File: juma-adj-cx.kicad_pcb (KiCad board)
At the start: 2 copper layers, 90 x 40 mm, 18 parts, among them J1 IN+, J2 IN-, J3 OUT+, J4 OUT-, Q1 BD139, Q2 2SC5200

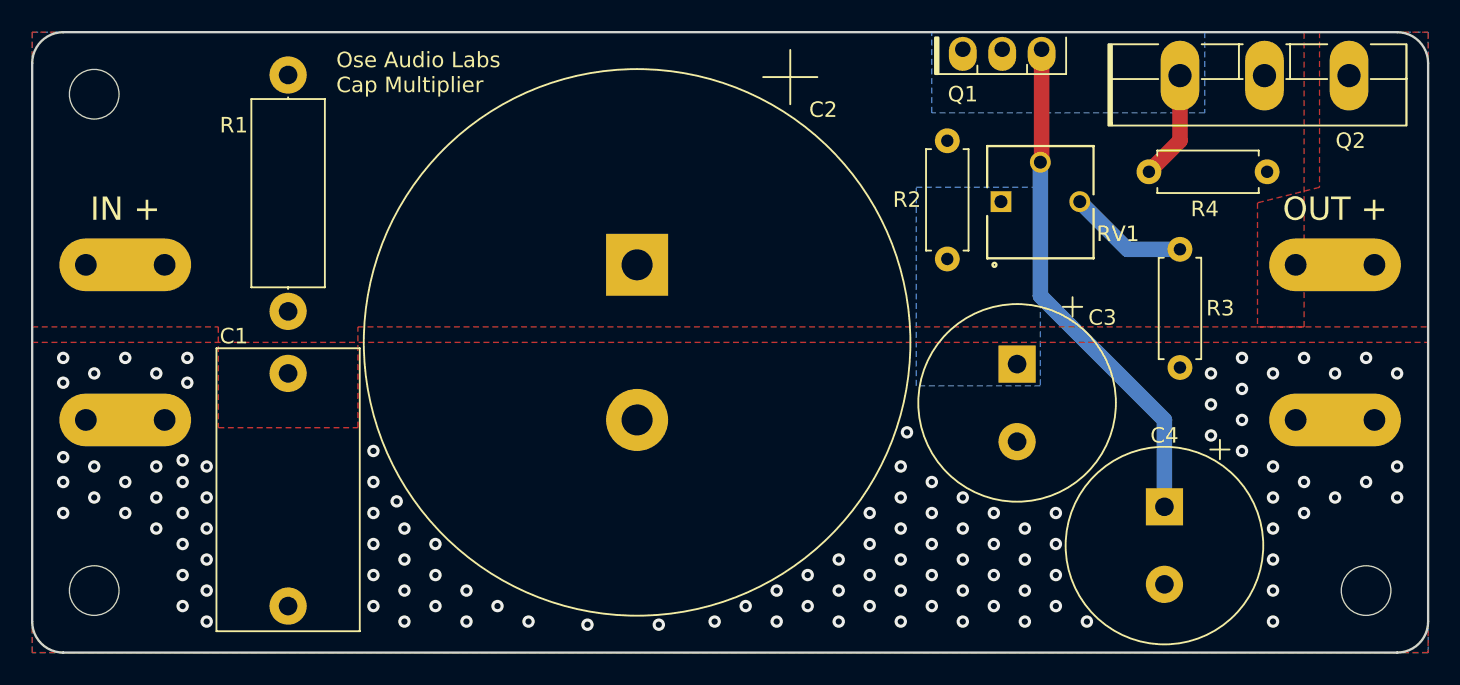
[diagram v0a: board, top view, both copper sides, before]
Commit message: separate in/out ground planes
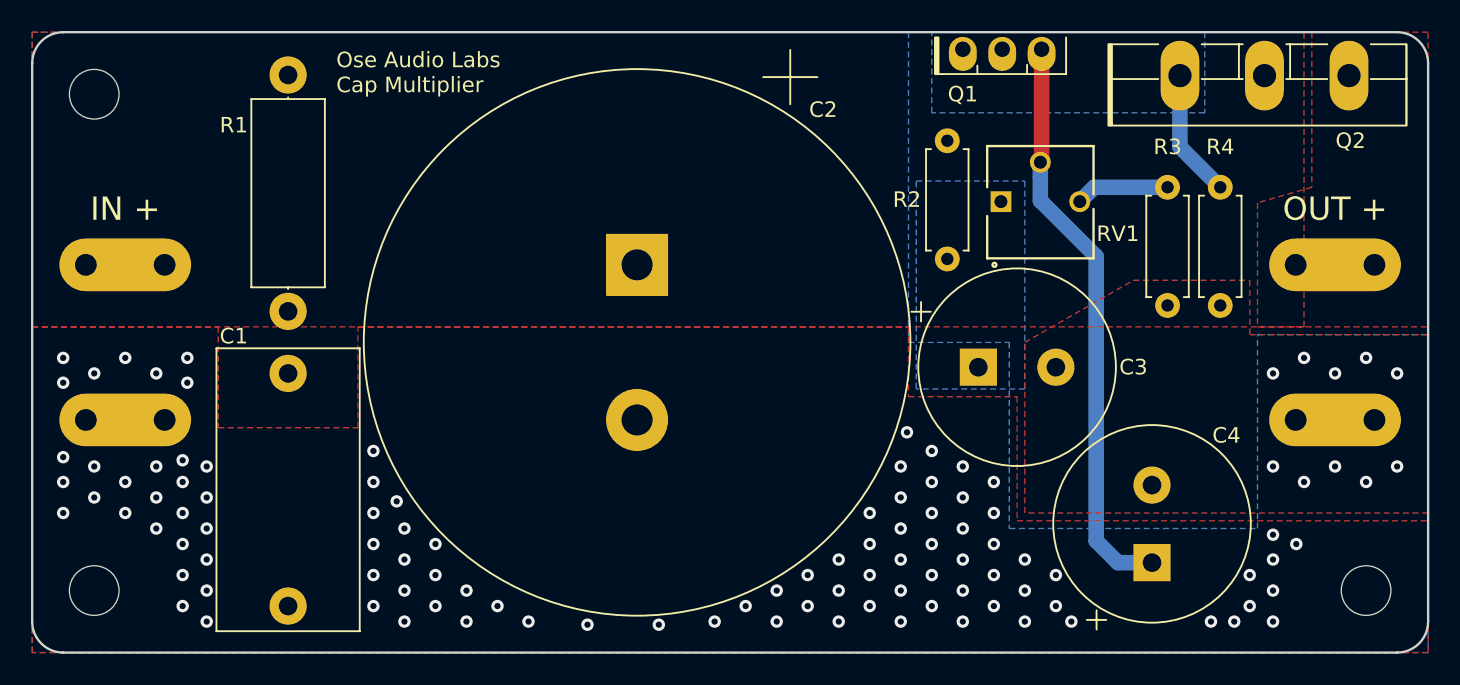
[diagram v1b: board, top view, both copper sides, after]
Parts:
- moved R4 4.71 mm to (156.6, 100.0), turned to 270 degrees
- moved R3 4.08 mm to (153.2, 100.0)
- moved C4 3.69 mm to (152.2, 124.2), turned to 90 degrees
- moved C3 2.51 mm to (141.0, 111.6), turned to 0 degrees
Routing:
- net Net-(C4-Pad1): track 32.8 -> 37.4 mm
- net Net-(R3-Pad1): track 7.73 -> 6.04 mm
- net Net-(Q1-Pad1): track 7.03 -> 8.28 mm
- net Net-(C1-Pad2): vias 116 -> 111

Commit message: mark j comment tweak
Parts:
- moved C4 4.07 mm to (150.5, 120.5), turned to 0 degrees
- moved J2 1.00 mm to (86.0, 114.0)
- moved J4 1.00 mm to (164.0, 114.0)
- moved C3 0.20 mm to (140.8, 111.6)
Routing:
- net Net-(C4-Pad1): track 37.4 -> 31.7 mm
- net Net-(C1-Pad2): vias 111 -> 134

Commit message: v1 for fab
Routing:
- net Net-(C1-Pad2): vias 134 -> 129
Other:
- board text added: "Ose Audio Labs Adjustable BJT Capacitance Multiplier github.com/oseaudiolabs/adjustable-cap-mx thx: AndrewT, Mark Johnson, prasi, xrk971"
- board text removed: "Ose Audio Labs Cap Multiplier"
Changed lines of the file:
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@@
     (thickness 1.6)
     (drawings 19)
-    (tracks 143)
+    (tracks 138)
     (zones 0)
     (modules 18)
@@
   (page A4)
   (layers
-    (0 F.Cu signal hide)
+    (0 F.Cu signal)
     (31 B.Cu signal)
     (32 B.Adhes user hide)
@@
     (34 B.Paste user hide)
     (35 F.Paste user hide)
-    (36 B.SilkS user hide)
-    (37 F.SilkS user hide)
-    (38 B.Mask user hide)
+    (36 B.SilkS user)
+    (37 F.SilkS user)
+    (38 B.Mask user)
     (39 F.Mask user)
     (40 Dwgs.User user hide)
@@
     (pcbplotparams
       (layerselection 0x010fc_ffffffff)
-      (usegerberextensions false)
+      (usegerberextensions true)
       (usegerberattributes false)
       (usegerberadvancedattributes false)
@@
       (psa4output false)
       (plotreference true)
-      (plotvalue true)
+      (plotvalue false)
       (plotinvisibletext false)
       (padsonsilk false)
@@
       (outputformat 1)
       (mirror false)
-      (drillshape 1)
+      (drillshape 0)
       (scaleselection 1)
-      (outputdirectory ""))
+      (outputdirectory "gerbers"))
   )
   (net 0 "")
@@
     (pad 1 np_thru_hole circle (at 0 0) (size 3.2 3.2) (drill 3.2) (layers *.Cu *.Mask))
   )
+  (gr_text "Ose Audio Labs\nAdjustable BJT Capacitance Multiplier\ngithub.com/oseaudiolabs/adjustable-cap-mx\n\nthx: AndrewT, Mark Johnson, prasi, xrk971" (at 135 96) (layer B.SilkS)
+    (effects (font (size 1 1) (thickness 0.14)) (justify left mirror))
+  )
   (dimension 32 (width 0.3) (layer F.Fab)
     (gr_text "32.000 mm" (at 73.9 110 270) (layer F.Fab)
@@
   (gr_arc (start 168 92) (end 170 92) (angle -90) (layer Edge.Cuts) (width 0.15))
   (gr_arc (start 82 92) (end 82 90) (angle -90) (layer Edge.Cuts) (width 0.15))
-  (gr_text "Ose Audio Labs\nCap Multiplier" (at 99.6 92.6) (layer F.SilkS)
-    (effects (font (size 1 1) (thickness 0.25)) (justify left))
-  )
   (gr_text "OUT +" (at 164 101.4) (layer F.SilkS)
     (effects (font (size 1.5 1.5) (thickness 0.3)))
@@
   (via (at 166 110) (size 0.8) (drill 0.4) (layers F.Cu B.Cu) (net 2))
   (via (at 168 111) (size 0.8) (drill 0.4) (layers F.Cu B.Cu) (net 2))
-  (via (at 136.4 115.8) (size 0.8) (drill 0.4) (layers F.Cu B.Cu) (net 2))
   (via (at 84 118) (size 0.8) (drill 0.4) (layers F.Cu B.Cu) (net 2))
   (via (at 88 118) (size 0.8) (drill 0.4) (layers F.Cu B.Cu) (net 2))
@@
   (via (at 88 120) (size 0.8) (drill 0.4) (layers F.Cu B.Cu) (net 2))
   (via (at 102 119) (size 0.8) (drill 0.4) (layers F.Cu B.Cu) (net 2))
-  (via (at 104 120.25) (size 0.8) (drill 0.4) (layers F.Cu B.Cu) (net 2))
   (via (at 136 120) (size 0.8) (drill 0.4) (layers F.Cu B.Cu) (net 2))
   (via (at 138 119) (size 0.8) (drill 0.4) (layers F.Cu B.Cu) (net 2))
@@
   (via (at 82 121) (size 0.8) (drill 0.4) (layers F.Cu B.Cu) (net 2))
   (via (at 82 119) (size 0.8) (drill 0.4) (layers F.Cu B.Cu) (net 2))
-  (via (at 82 117.4) (size 0.8) (drill 0.4) (layers F.Cu B.Cu) (net 2))
+  (via (at 82 117) (size 0.8) (drill 0.4) (layers F.Cu B.Cu) (net 2))
   (via (at 82 112) (size 0.8) (drill 0.4) (layers F.Cu B.Cu) (net 2))
   (via (at 82 110) (size 0.8) (drill 0.4) (layers F.Cu B.Cu) (net 2))
@@
   (via (at 90 123) (size 0.8) (drill 0.4) (layers F.Cu B.Cu) (net 2))
   (via (at 90 129) (size 0.8) (drill 0.4) (layers F.Cu B.Cu) (net 2))
-  (via (at 160 119) (size 0.8) (drill 0.4) (layers F.Cu B.Cu) (net 2))
-  (via (at 164 119) (size 0.8) (drill 0.4) (layers F.Cu B.Cu) (net 2))
-  (via (at 168 119) (size 0.8) (drill 0.4) (layers F.Cu B.Cu) (net 2))
   (via (at 160 122) (size 0.8) (drill 0.4) (layers F.Cu B.Cu) (net 2))
   (via (at 162 121) (size 0.8) (drill 0.4) (layers F.Cu B.Cu) (net 2))
@@
     (connect_pads yes (clearance 0.254))
     (min_thickness 0.254)
-    (fill yes (arc_segments 16) (thermal_gap 0.508) (thermal_bridge_width 0.508))
+    (fill yes (arc_segments 16) (thermal_gap 0.508) (thermal_bridge_width 0.508) (smoothing fillet) (radius 0.5))
     (polygon
       (pts
@@
     (polygon
       (pts
-        (xy 144 99.6) (xy 144 113) (xy 137 113) (xy 137 99.6)
+        (xy 143.5 99.6) (xy 143.5 113) (xy 137 113) (xy 137 99.6)
       )
     )
